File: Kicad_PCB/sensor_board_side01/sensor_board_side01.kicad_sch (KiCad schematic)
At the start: 1 part, among them J1 Conn_01x06_Female

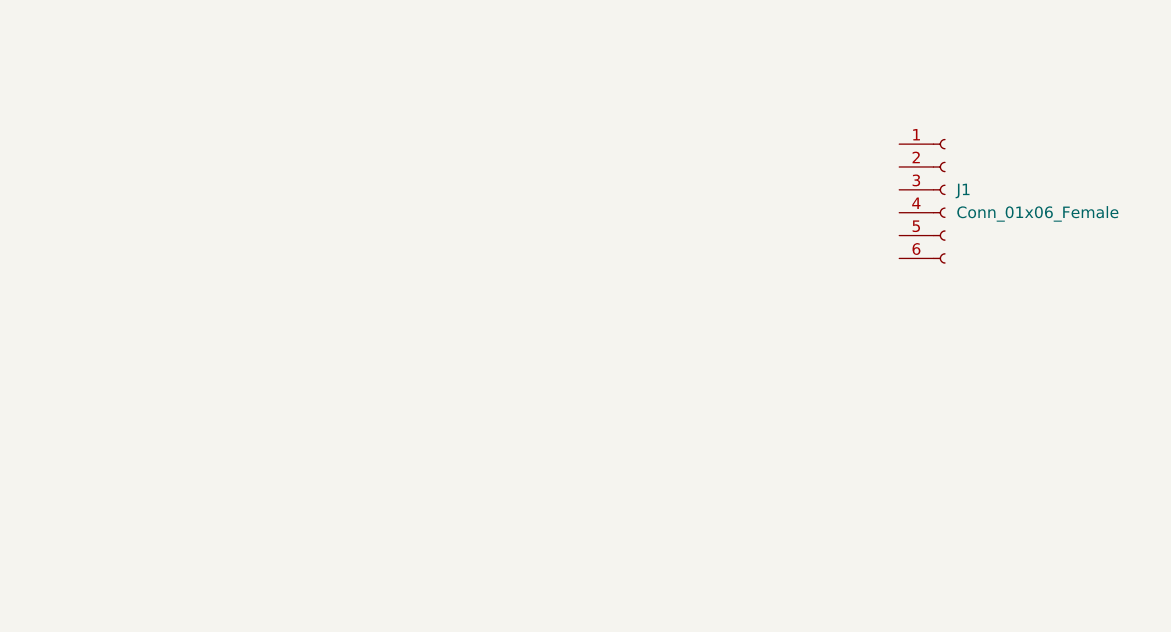
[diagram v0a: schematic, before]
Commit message: ohmmeter circuit
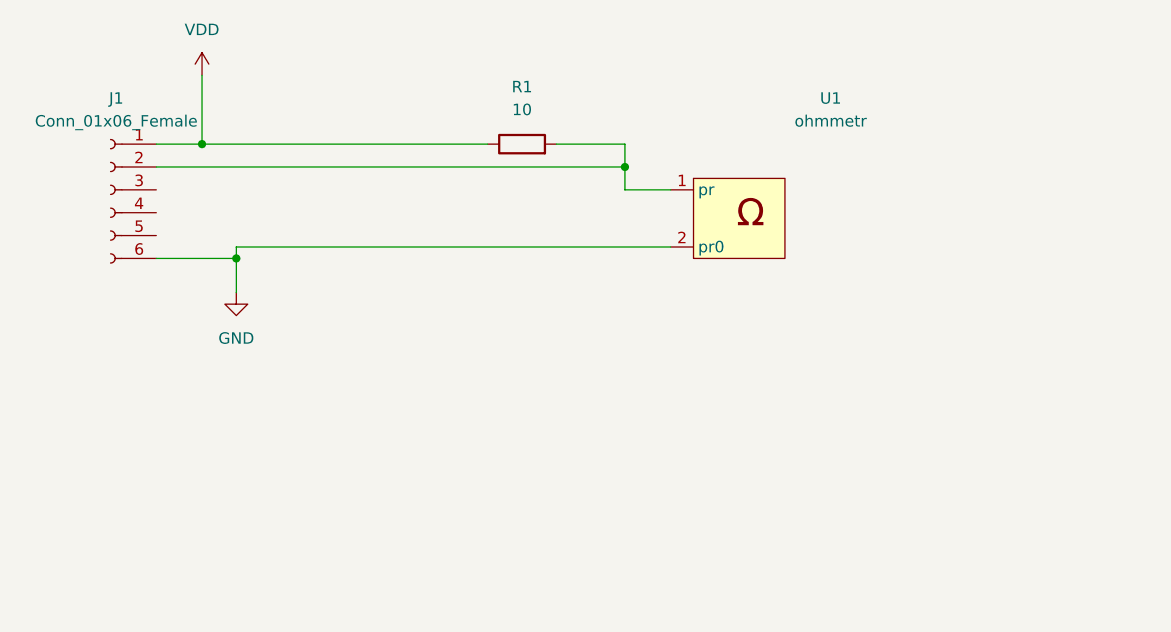
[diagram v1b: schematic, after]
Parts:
- added R1: 10, Resistor_SMD:R_0402_1005Metric, symbol Device:R
- added U1: ohmmetr, ohm_metr:ohm_metr, symbol ohmmetr:ohmmetr
- J1: footprint (none) -> Connector_Hirose:Hirose_DF13-06P-1.25DSA_1x06_P1.25mm_Vertical
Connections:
- net VDD: now reaches J1.1 (Pin_1)
- net VDD: now also R1.1
- net at J1.2 (Pin_2): now also R1.2, U1.1 (pr)
- net GND: now reaches J1.6 (Pin_6)
- net GND: now also U1.2 (pr0)
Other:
- moved on the sheet: J1
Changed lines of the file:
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@@
 (kicad_sch (version 20211123) (generator eeschema)
   (paper "A4")
-  (symbol (lib_id "Connector:Conn_01x06_Female") (at 196.85 114.3 0) (unit 1)
+  (junction (at 118.11 121.92) (diameter 0) (color 0 0 0 0)
+  )
+  (junction (at 114.3 109.22) (diameter 0) (color 0 0 0 0)
+  )
+  (junction (at 161.29 111.76) (diameter 0) (color 0 0 0 0)
+  )
+  (wire (pts (xy 109.22 121.92) (xy 118.11 121.92))
+    (stroke (width 0) (type default) (color 0 0 0 0))
+  )
+  (wire (pts (xy 118.11 120.65) (xy 118.11 121.92))
+    (stroke (width 0) (type default) (color 0 0 0 0))
+  )
+  (wire (pts (xy 161.29 111.76) (xy 161.29 114.3))
+    (stroke (width 0) (type default) (color 0 0 0 0))
+  )
+  (wire (pts (xy 161.29 114.3) (xy 166.37 114.3))
+    (stroke (width 0) (type default) (color 0 0 0 0))
+  )
+  (wire (pts (xy 114.3 109.22) (xy 146.05 109.22))
+    (stroke (width 0) (type default) (color 0 0 0 0))
+  )
+  (wire (pts (xy 153.67 109.22) (xy 161.29 109.22))
+    (stroke (width 0) (type default) (color 0 0 0 0))
+  )
+  (wire (pts (xy 109.22 111.76) (xy 161.29 111.76))
+    (stroke (width 0) (type default) (color 0 0 0 0))
+  )
+  (wire (pts (xy 118.11 120.65) (xy 166.37 120.65))
+    (stroke (width 0) (type default) (color 0 0 0 0))
+  )
+  (wire (pts (xy 114.3 101.6) (xy 114.3 109.22))
+    (stroke (width 0) (type default) (color 0 0 0 0))
+  )
+  (wire (pts (xy 109.22 109.22) (xy 114.3 109.22))
+    (stroke (width 0) (type default) (color 0 0 0 0))
+  )
+  (wire (pts (xy 118.11 121.92) (xy 118.11 125.73))
+    (stroke (width 0) (type default) (color 0 0 0 0))
+  )
+  (wire (pts (xy 161.29 109.22) (xy 161.29 111.76))
+    (stroke (width 0) (type default) (color 0 0 0 0))
+  )
+  (symbol (lib_id "power:GND") (at 118.11 125.73 0) (unit 1)
     (in_bom yes) (on_board yes) (fields_autoplaced)
-    (property "Reference" "J1" (id 0) (at 198.12 114.2999 0)
-      (effects (font (size 1.27 1.27)) (justify left))
-    )
-    (property "Value" "Conn_01x06_Female" (id 1) (at 198.12 116.8399 0)
-      (effects (font (size 1.27 1.27)) (justify left))
-    )
-    (property "Footprint" "" (id 2) (at 196.85 114.3 0)
+    (property "Reference" "#PWR02" (id 0) (at 118.11 132.08 0)
       (effects (font (size 1.27 1.27)) hide)
     )
-    (property "Datasheet" "~" (id 3) (at 196.85 114.3 0)
+    (property "Value" "GND" (id 1) (at 118.11 130.81 0))
+    (property "Footprint" "" (id 2) (at 118.11 125.73 0)
+      (effects (font (size 1.27 1.27)) hide)
+    )
+    (property "Datasheet" "" (id 3) (at 118.11 125.73 0)
+      (effects (font (size 1.27 1.27)) hide)
+    )
+    (pin "1")
+  )
+  (symbol (lib_id "Connector:Conn_01x06_Female") (at 104.14 114.3 0) (mirror y) (unit 1)
+    (in_bom yes) (on_board yes) (fields_autoplaced)
+    (property "Reference" "J1" (id 0) (at 104.775 104.14 0))
+    (property "Value" "Conn_01x06_Female" (id 1) (at 104.775 106.68 0))
+    (property "Footprint" "Connector_Hirose:Hirose_DF13-06P-1.25DSA_1x06_P1.25mm_Vertical" (id 2) (at 104.14 114.3 0)
+      (effects (font (size 1.27 1.27)) hide)
+    )
+    (property "Datasheet" "~" (id 3) (at 104.14 114.3 0)
       (effects (font (size 1.27 1.27)) hide)
     )
@@
     (pin "6")
   )
+  (symbol (lib_id "ohmmetr:ohmmetr") (at 166.37 120.65 0) (unit 1)
+    (in_bom yes) (on_board yes) (fields_autoplaced)
+    (property "Reference" "U1" (id 0) (at 184.15 104.14 0))
+    (property "Value" "ohmmetr" (id 1) (at 184.15 106.68 0))
+    (property "Footprint" "ohm_metr:ohm_metr" (id 2) (at 167.64 123.19 0)
+      (effects (font (size 1.27 1.27)) hide)
+    )
+    (property "Datasheet" "" (id 3) (at 166.37 120.65 0)
+      (effects (font (size 1.27 1.27)) hide)
+    )
+    (pin "2")
+    (pin "1")
+  )
+  (symbol (lib_id "Device:R") (at 149.86 109.22 90) (unit 1)
+    (in_bom yes) (on_board yes) (fields_autoplaced)
+    (property "Reference" "R1" (id 0) (at 149.86 102.87 90))
+    (property "Value" "10" (id 1) (at 149.86 105.41 90))
+    (property "Footprint" "Resistor_SMD:R_0402_1005Metric" (id 2) (at 149.86 110.998 90)
+      (effects (font (size 1.27 1.27)) hide)
+    )
+    (property "Datasheet" "~" (id 3) (at 149.86 109.22 0)
+      (effects (font (size 1.27 1.27)) hide)
+    )
+    (pin "1")
+    (pin "2")
+  )
+  (symbol (lib_id "power:VDD") (at 114.3 101.6 0) (unit 1)
+    (in_bom yes) (on_board yes) (fields_autoplaced)
+    (property "Reference" "#PWR01" (id 0) (at 114.3 105.41 0)
+      (effects (font (size 1.27 1.27)) hide)
+    )
+    (property "Value" "VDD" (id 1) (at 114.3 96.52 0))
+    (property "Footprint" "" (id 2) (at 114.3 101.6 0)
+      (effects (font (size 1.27 1.27)) hide)
+    )
+    (property "Datasheet" "" (id 3) (at 114.3 101.6 0)
+      (effects (font (size 1.27 1.27)) hide)
+    )
+    (pin "1")
+  )
   (sheet_instances
     (path "/" (page "1"))
   )
   (symbol_instances
+    (path "/c3374400-48ea-4594-9062-d76c4c5c9cde"
+      (reference "#PWR01") (unit 1) (value "VDD") (footprint "")
+    )
+    (path "/00f241f0-c742-4247-b438-534f7979b420"
+      (reference "#PWR02") (unit 1) (value "GND") (footprint "")
+    )
     (path "/679bc502-9a00-42cb-a2db-58ce09e9a170"
       (reference "J1") (unit 1) (value "Conn_01x06_Female") (footprint "Connector_Hirose:Hirose_DF13-06P-1.25DSA_1x06_P1.25mm_Vertical")
     )
+    (path "/914cf001-04f0-4777-b3e6-e94723492083"
+      (reference "R1") (unit 1) (value "10") (footprint "Resistor_SMD:R_0402_1005Metric")
+    )
+    (path "/8206cd9e-3a29-4623-bf65-a9c214c04539"
+      (reference "U1") (unit 1) (value "ohmmetr") (footprint "ohm_metr:ohm_metr")
+    )
   )

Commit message: Sensor Board Schematic
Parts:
- added C1: 1uF, Capacitor_SMD:C_0805_2012Metric, symbol Device:C
- added C2: 0.1uF, Capacitor_SMD:C_0805_2012Metric, symbol Device:C
- added C3: 10nF, Capacitor_SMD:C_0805_2012Metric, symbol Device:C
- added R2: 1k, Resistor_SMD:R_0402_1005Metric, symbol Device:R
- added R3: 100k, Resistor_SMD:R_0402_1005Metric, symbol Device:R
- added R4: 1M, Resistor_SMD:R_0402_1005Metric, symbol Device:R
- added R5: 10k, Resistor_SMD:R_0402_1005Metric, symbol Device:R
- added U2: AT42QT1012-M, Package_DFN_QFN:DFN-8-1EP_2x2mm_P0.5mm_EP0.9x1.5mm, symbol Sensor_Touch:AT42QT1012-M
- added U3: sensor, cup_toch:toch_sens, symbol cap_touch:sensor
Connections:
- net GND: now also C1.2, C2.2, R2.1, R3.1, R4.1, U2.4 (VSS), U2.6 (TIME), U2.9 (VSS)
- net VDD: now also C2.1, U2.7 (VDD)
- net at J1.2 (Pin_2), R1.2, U1.1 (pr): now also C1.1, R2.2
- net at J1.3 (Pin_3): now also R3.2, U2.5 (OUT)
- new net: C3.1, R4.2, U2.8 (SNS)
- new net: C3.2, R5.1, U2.1 (SNSK)
- new net: R5.2, U3.1 (s)
